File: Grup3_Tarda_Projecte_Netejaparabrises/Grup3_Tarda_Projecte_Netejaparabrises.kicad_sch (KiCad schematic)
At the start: 0 parts

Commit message: canvis schematic 05-04-23
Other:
- note added: "SISTEMA DE NETEJAPARABRISES"
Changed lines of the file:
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@@
   (title_block
     (title "Projecte Netejaparabrises - Grup 4 Tarda")
-    (date "2023-03-30")
-    (rev "v1.0.30032023")
+    (date "2023-04-05")
+    (rev "v1.1.05042023")
   )
   (bus (pts (xy 285.75 100.33) (xy 285.75 123.19))
@@
     (effects (font (size 5 5) (thickness 1) bold) (justify left bottom))
   )
+  (text "SISTEMA DE NETEJAPARABRISES" (at 29.21 177.292 0)
+    (effects (font (size 5 5) (thickness 1) bold) (justify left bottom))
+  )

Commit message: canvis schematic i README 07-04-2023
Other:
- sheet Microcontrolador renamed Digital
- removed sheet Control i Alimentacio
- added sheet Alimentacio (Alimentacio.kicad_sch)
- sheet Potencia: file Alimentacio.kicad_sch -> Potencia.kicad_sch
- note added: "ALIMENTACIO"
- note added: "DRIVERS I MOTORS"
- note removed: "DRIVERS I ALIMENTACIO"
- note removed: "POTENCIA"
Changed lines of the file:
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@@
     (rev "v1.1.05042023")
-  )
-  (bus (pts (xy 285.75 100.33) (xy 285.75 123.19))
-    (stroke (width 0) (type default))
   )
   (polyline (pts (xy 285.75 43.18) (xy 285.75 48.26))
@@
     (effects (font (size 3 3)) (justify left top))
   )
-  (text_box "-Driver motor davant (motor 1)\n-Driver motor darrere (motor 2)\n-Driver bomba davant i darrer\n-Driver luneta termica"
-    (at 198.882 76.708 0) (size 77.724 26.67)
+  (text_box "-Driver motor davant (motor 1)\n-Driver motor darrere (motor 2)\n-Driver bomba davant i darrere\n-Driver luneta termica"
+    (at 198.628 65.278 0) (size 77.724 32.766)
     (stroke (width 0) (type default))
     (fill (type none))
@@
   )
   (text_box "-Microcontrolador\n-Entrades digitals\n-Comunicacions"
-    (at 102.616 76.708 0) (size 82.55 18.796)
+    (at 102.616 65.278 0) (size 82.55 18.796)
     (stroke (width 0) (type default))
     (fill (type none))
     (effects (font (size 3 3)) (justify left top))
   )
-  (text_box "-Regulaodor a 5V"
+  (text_box "-Regulador a 5V"
     (at 17.272 57.15 0) (size 69.85 11.43)
     (stroke (width 0) (type default))
@@
     (effects (font (size 5 5) (thickness 1) bold) (justify left bottom))
   )
-  (text "DRIVERS I\nALIMENTACIO" (at 199.39 58.42 0)
+  (text "DRIVERS I MOTORS" (at 199.136 52.832 0)
     (effects (font (size 5 5) (thickness 1) bold) (justify left bottom))
   )
-  (text "POTENCIA" (at 17.78 51.562 0)
+  (text "ALIMENTACIO" (at 17.78 51.562 0)
     (effects (font (size 5 5) (thickness 1) bold) (justify left bottom))
   )
@@
     (stroke (width 0.1524) (type solid))
     (fill (color 0 0 0 0.0000))
-    (property "Sheetname" "Microcontrolador" (at 98.806 15.5444 0)
+    (property "Sheetname" "Digital" (at 98.806 15.5444 0)
       (effects (font (size 1.27 1.27)) (justify left bottom))
     )
@@
     (stroke (width 0.1524) (type solid))
     (fill (color 0 0 0 0.0000))
-    (property "Sheetname" "Control i Alimentacio" (at 195.326 15.5444 0)
+    (property "Sheetname" "Potencia" (at 195.326 15.5444 0)
       (effects (font (size 1.27 1.27)) (justify left bottom))
     )
@@
     (stroke (width 0.1524) (type solid))
     (fill (color 0 0 0 0.0000))
-    (property "Sheetname" "Potencia" (at 15.24 15.0364 0)
+    (property "Sheetname" "Alimentacio" (at 15.24 15.0364 0)
       (effects (font (size 1.27 1.27)) (justify left bottom))
     )

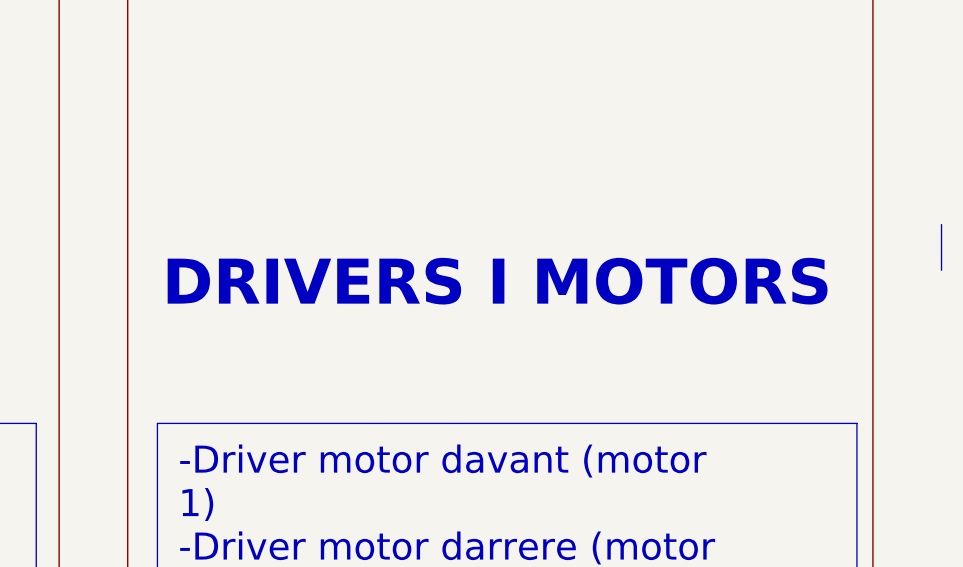
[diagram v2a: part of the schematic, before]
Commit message: canvis menors a esquematic i README
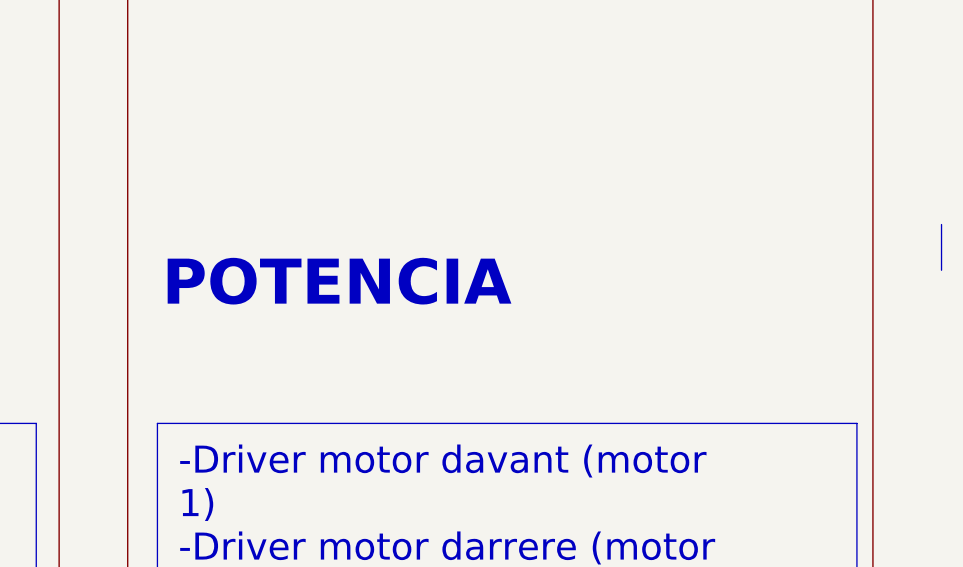
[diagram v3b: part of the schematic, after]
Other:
- note added: "POTENCIA"
- note removed: "DRIVERS I MOTORS"
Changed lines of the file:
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@@
     (effects (font (size 5 5) (thickness 1) bold) (justify left bottom))
   )
-  (text "DRIVERS I MOTORS" (at 199.136 52.832 0)
+  (text "POTENCIA" (at 199.136 52.832 0)
     (effects (font (size 5 5) (thickness 1) bold) (justify left bottom))
   )
